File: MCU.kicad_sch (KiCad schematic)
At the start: 39 parts, among them J1 JTAG, J2 HH-16P-CB-TYPE-C, J3 GPS, J4 CAM, J5 GPS, J6 CAM, SW1 TS2306A, U4 RP2354A, U5 W25Q128JVPIQ, U6 USBLC6-2P6, Y1 12MHz

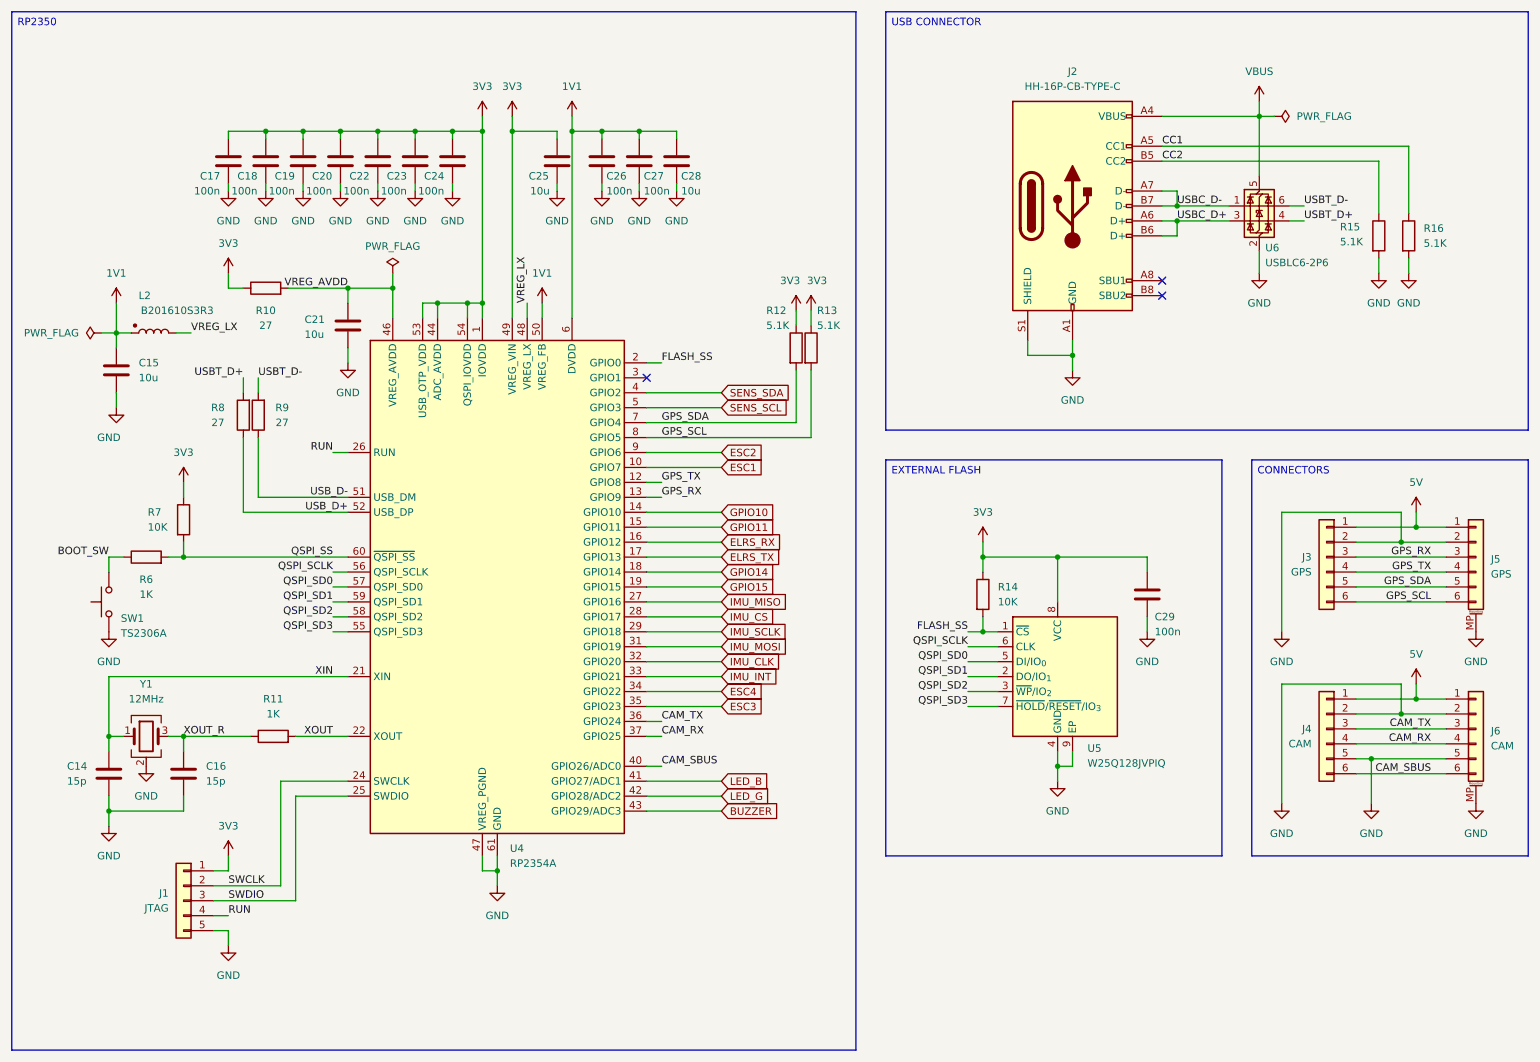
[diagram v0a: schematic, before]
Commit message: Oscillator and IMU layout
Updated the oscillator layout for the RP2350.
Updated the IMU layout for the IMU.
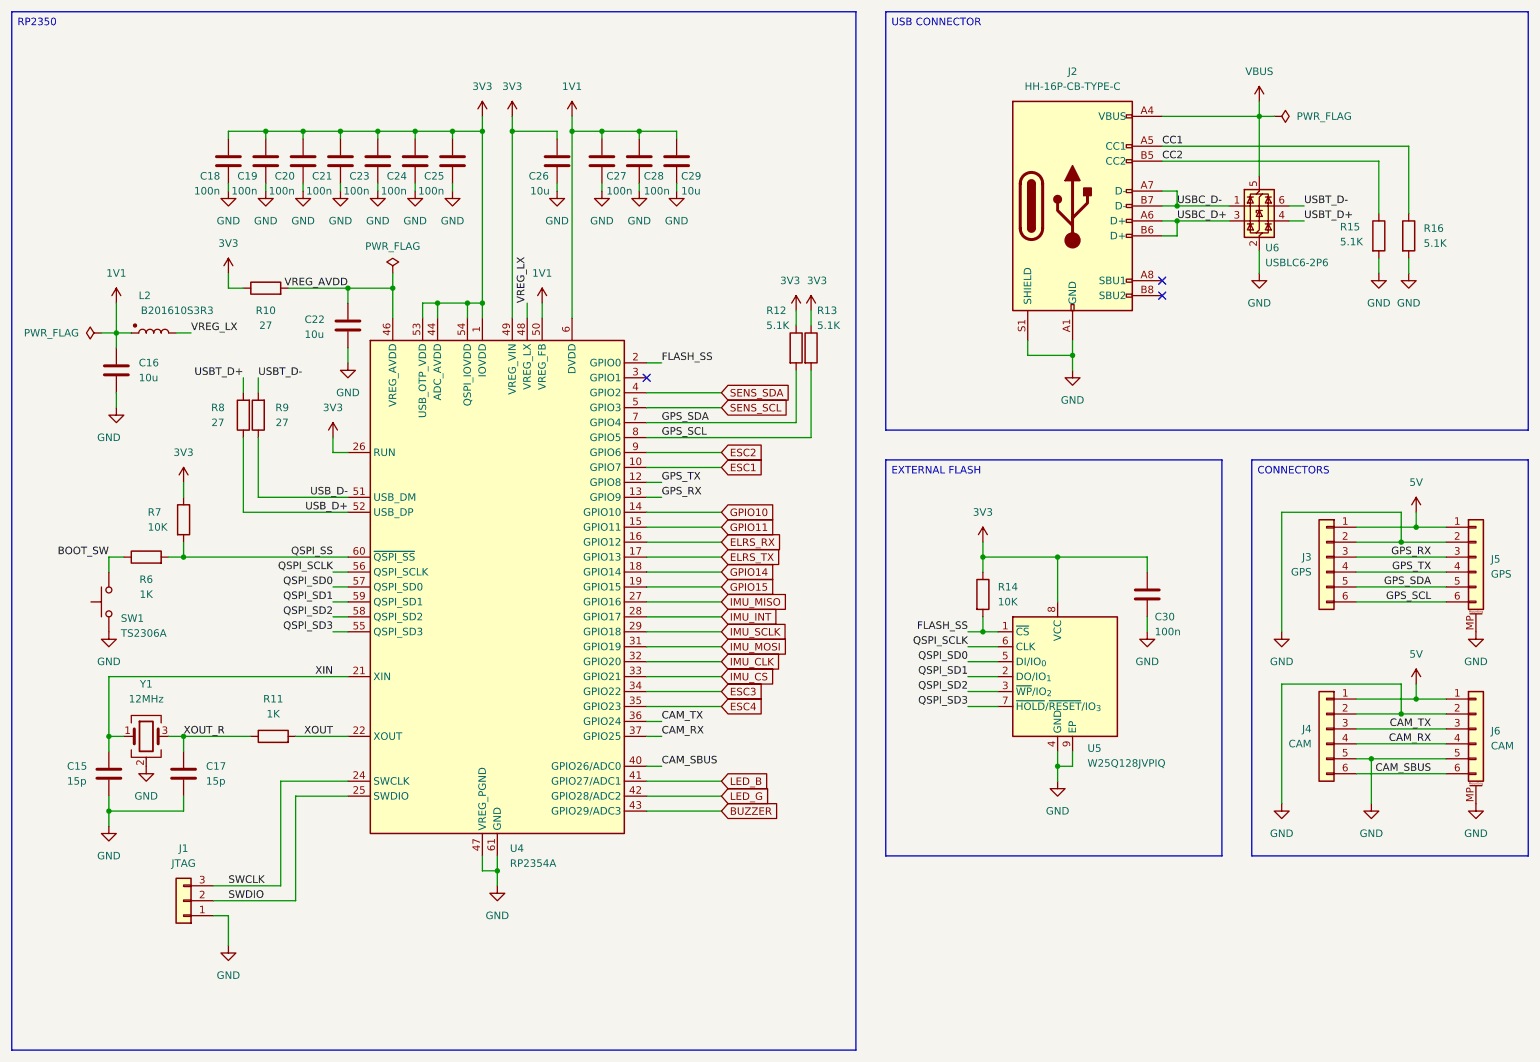
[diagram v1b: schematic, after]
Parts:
- removed J1: JTAG, Custom_Parts:PAD_5_SQUARE_SOLID_1.0x1.0mm_P1.5mm, symbol Connector_Generic:Conn_01x05
- added J1: JTAG, Custom_Parts:PAD_3_SQUARE_SOLID_1.0x1.0mm_P1.5mm, symbol Connector_Generic:Conn_01x03
- renumbered C14 to C15, C15 to C16, C16 to C17, C17 to C18, C18 to C19, C19 to C20, C20 to C21, C21 to C22, C22 to C23, C23 to C24, C24 to C25, C25 to C26, C26 to C27, C27 to C28, C28 to C29, C29 to C30
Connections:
- net RUN is gone; now on net 3V3: U4.26 (RUN)
- net ESC3: now also U4.34 (GPIO22); no longer U4.35 (GPIO23)
- net ESC4: now also U4.35 (GPIO23); no longer U4.34 (GPIO22)
- net GND: now also J1.1 (Pin_1)
- net IMU_CS: now also U4.33 (GPIO21); no longer U4.28 (GPIO17)
- net IMU_INT: now also U4.28 (GPIO17); no longer U4.33 (GPIO21)
- net SWCLK: now also J1.3 (Pin_3)
- net SWDIO: now also J1.2 (Pin_2)

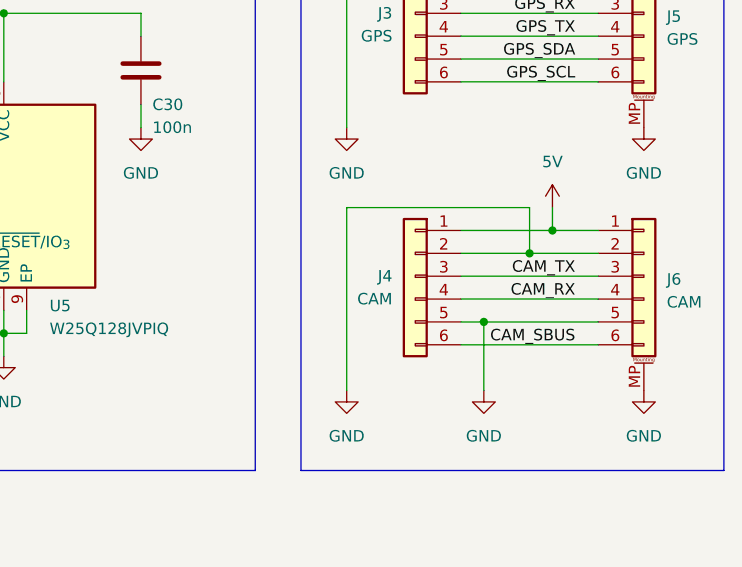
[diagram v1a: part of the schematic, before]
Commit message: ESC layout and connections
Updated an alignment issue with some ESC layouts.
Added power connections.
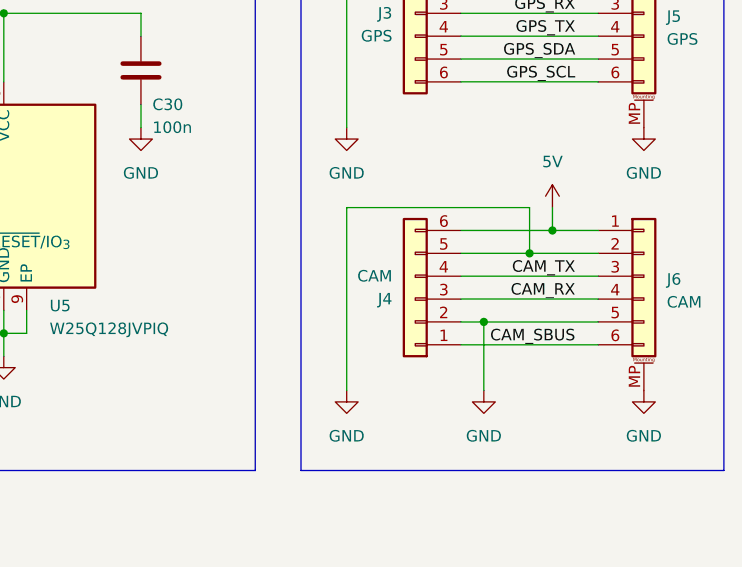
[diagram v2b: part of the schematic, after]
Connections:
- net 5V: now also J4.6 (Pin_6); no longer J4.1 (Pin_1)
- net CAM_RX: now also J4.3 (Pin_3); no longer J4.4 (Pin_4)
- net CAM_SBUS: now also J4.1 (Pin_1); no longer J4.6 (Pin_6)
- net CAM_TX: now also J4.4 (Pin_4); no longer J4.3 (Pin_3)
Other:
- moved on the sheet: J4
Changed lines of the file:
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@@
 	(symbol
 		(lib_id "Connector_Generic:Conn_01x06")
-		(at 243.84 138.43 0)
-		(mirror y)
+		(at 243.84 140.97 180)
 		(unit 1)
 		(exclude_from_sim no)
@@
 		(dnp no)
 		(property "Reference" "J4"
-			(at 241.3 138.4299 0)
+			(at 241.3 140.9701 0)
 			(effects
 				(font
@@
 		)
 		(property "Value" "CAM"
-			(at 241.3 140.9699 0)
+			(at 241.3 138.4301 0)
 			(effects
 				(font
@@
 		)
 		(property "Footprint" "Custom_Parts:PAD_6_SQUARE_SOLID_1.5x1.5mm_P2.0mm"
-			(at 243.84 138.43 0)
+			(at 243.84 140.97 0)
 			(effects
 				(font
@@
 		)
 		(property "Datasheet" "~"
-			(at 243.84 138.43 0)
+			(at 243.84 140.97 0)
 			(effects
 				(font
@@
 		)
 		(property "Description" "Generic connector, single row, 01x06, script generated (kicad-library-utils/schlib/autogen/connector/)"
-			(at 243.84 138.43 0)
+			(at 243.84 140.97 0)
 			(effects
 				(font

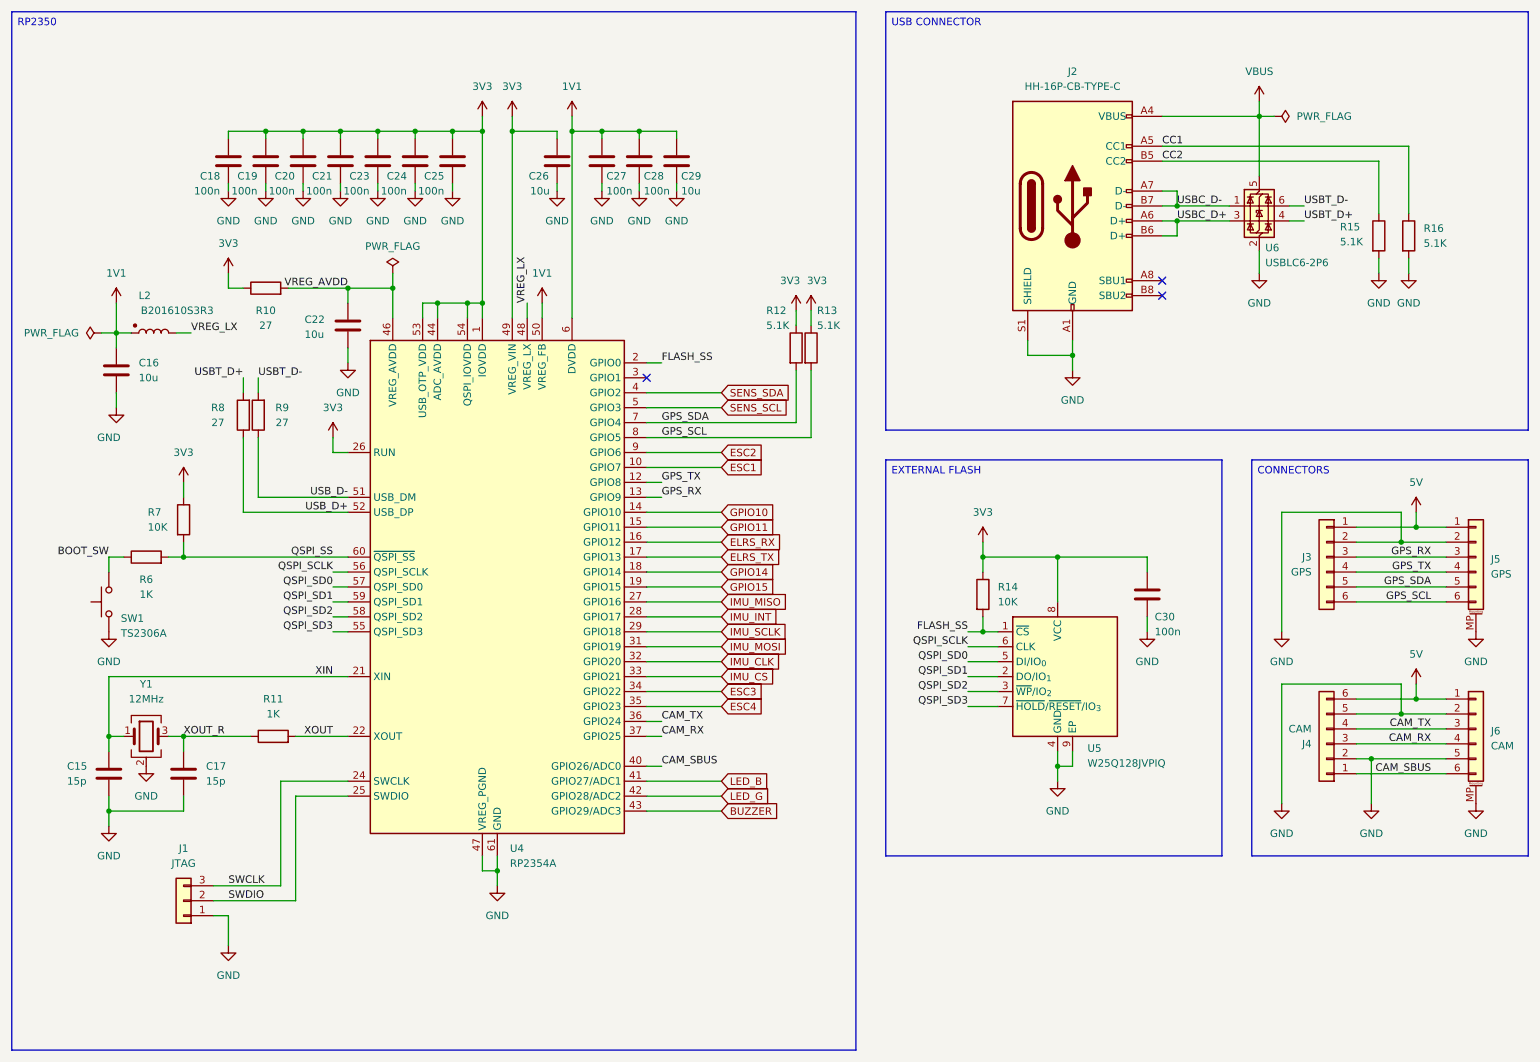
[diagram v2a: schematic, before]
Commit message: Voltage detection
Added a VBUS voltage detection for the RP.
Minor layout changes.
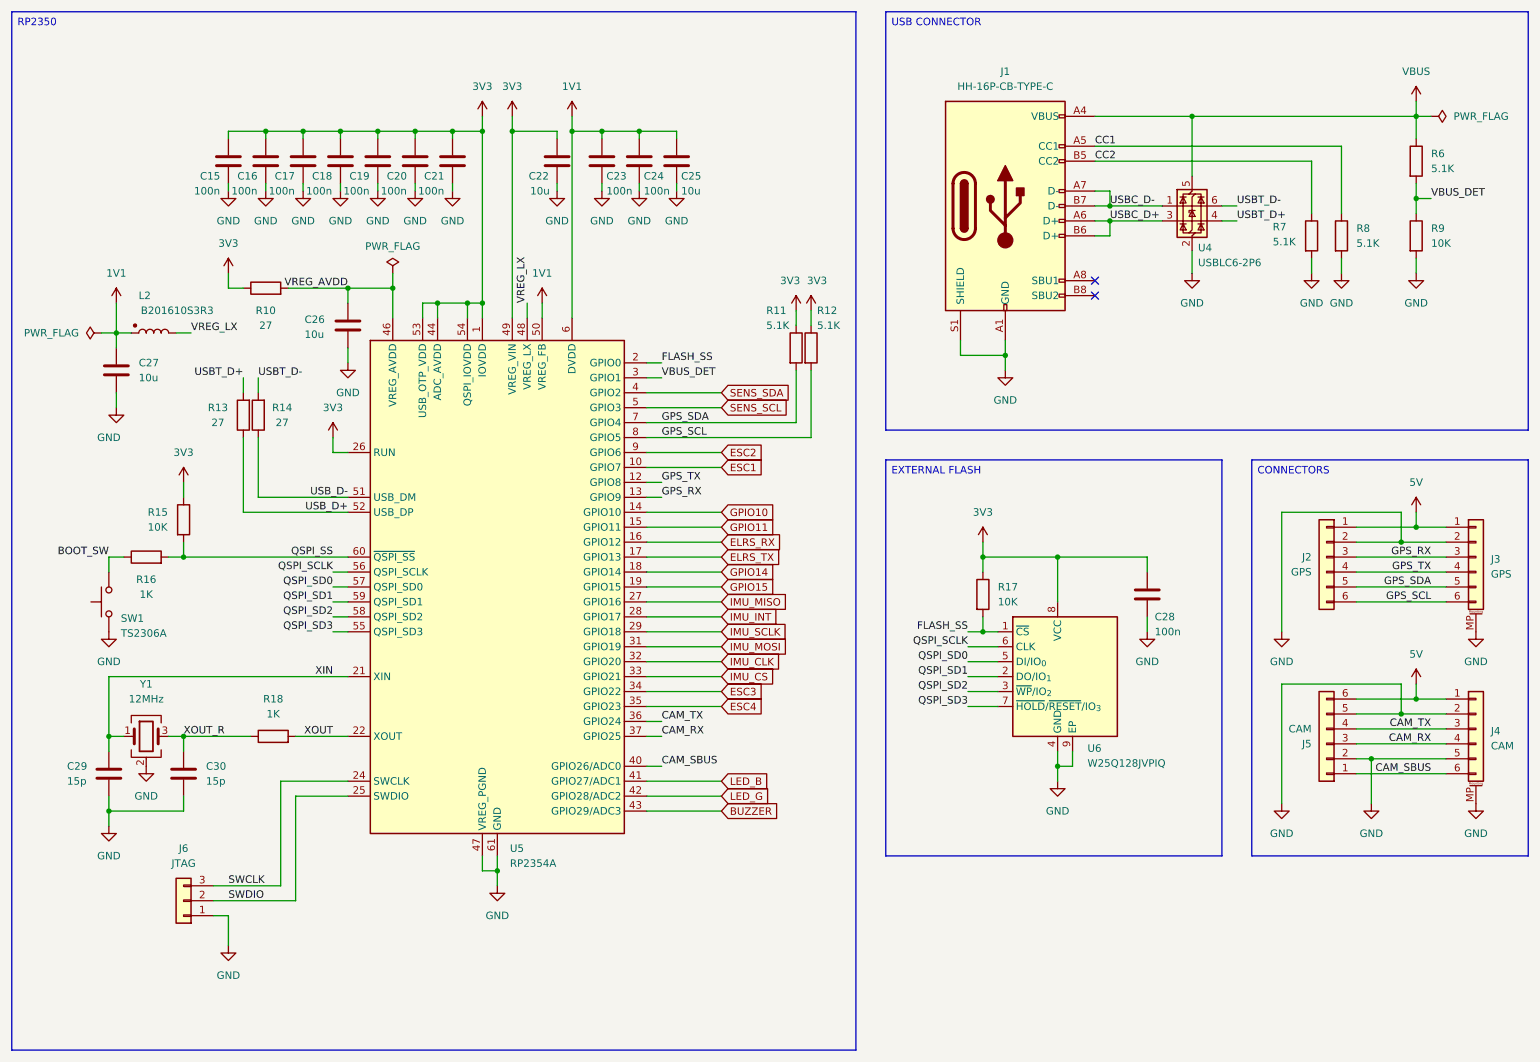
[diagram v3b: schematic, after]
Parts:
- added R6: 5.1K, Resistor_SMD:R_0603_1608Metric, symbol Device:R
- added R9: 10K, Resistor_SMD:R_0603_1608Metric, symbol Device:R
- renumbered C18 to C15, C19 to C16, C20 to C17, C21 to C18, C23 to C19, C24 to C20, C25 to C21, C26 to C22, C27 to C23, C28 to C24, C29 to C25, C22 to C26, C16 to C27, C30 to C28, C15 to C29, C17 to C30, J2 to J1, J3 to J2, J5 to J3, J6 to J4, J4 to J5, J1 to J6, R12 to R11, R13 to R12, R8 to R13, R9 to R14, R7 to R15, R6 to R16, R14 to R17, R11 to R18, R15 to R7, R16 to R8, U6 to U4, U4 to U5, U5 to U6
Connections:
- net GND: now also R9.2
- net VBUS: now also R6.1
- net VBUS_DET: now reaches U5.3 (GPIO1)
- net VBUS_DET: now also R6.2, R9.1
- no-connect marks 3 -> 2
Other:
- moved on the sheet: J1, R7, R8, U4
